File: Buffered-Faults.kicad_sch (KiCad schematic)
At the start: 4 parts, among them U6 TSB712AIDT, U7 TSB712AIDT

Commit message: completed placement:
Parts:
- renumbered U6 to U7, U7 to U8
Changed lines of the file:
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@@
 		(on_board yes)
 		(dnp no)
-		(property "Reference" "#PWR06"
+		(property "Reference" "#PWR0101"
 			(at 240.03 133.35 0)
 			(effects
@@
 			(project "Shutdown"
 				(path "/624b8e71-6fec-49ba-b7c9-b659e140fc2f/d0efc49a-1e04-47b9-bbf8-a506e96d4b4f"
-					(reference "#PWR06")
+					(reference "#PWR0101")
 					(unit 1)
 				)
@@
 		(dnp no)
 		(fields_autoplaced yes)
-		(property "Reference" "U6"
+		(property "Reference" "U7"
 			(at 255.27 124.46 0)
 			(effects
@@
 			(project "Shutdown"
 				(path "/624b8e71-6fec-49ba-b7c9-b659e140fc2f/d0efc49a-1e04-47b9-bbf8-a506e96d4b4f"
-					(reference "U6")
+					(reference "U7")
 					(unit 3)
 				)
@@
 		(on_board yes)
 		(dnp no)
-		(property "Reference" "#PWR0105"
+		(property "Reference" "#PWR0104"
 			(at 240.03 185.42 0)
 			(effects
@@
 			(project "Shutdown"
 				(path "/624b8e71-6fec-49ba-b7c9-b659e140fc2f/d0efc49a-1e04-47b9-bbf8-a506e96d4b4f"
-					(reference "#PWR0105")
+					(reference "#PWR0104")
 					(unit 1)
 				)
@@
 		(dnp no)
 		(fields_autoplaced yes)
-		(property "Reference" "U6"
+		(property "Reference" "U7"
 			(at 180.975 93.98 0)
 			(effects
@@
 			(project "Shutdown"
 				(path "/624b8e71-6fec-49ba-b7c9-b659e140fc2f/d0efc49a-1e04-47b9-bbf8-a506e96d4b4f"
-					(reference "U6")
+					(reference "U7")
 					(unit 1)
 				)
@@
 		(dnp no)
 		(fields_autoplaced yes)
-		(property "Reference" "U7"
+		(property "Reference" "U8"
 			(at 180.975 154.94 0)
 			(effects
@@
 			(project "Shutdown"
 				(path "/624b8e71-6fec-49ba-b7c9-b659e140fc2f/d0efc49a-1e04-47b9-bbf8-a506e96d4b4f"
-					(reference "U7")
+					(reference "U8")
 					(unit 1)
 				)
@@
 		(on_board yes)
 		(dnp no)
-		(property "Reference" "#PWR010"
+		(property "Reference" "#PWR0102"
 			(at 240.03 151.13 0)
 			(effects
@@
 			(project "Shutdown"
 				(path "/624b8e71-6fec-49ba-b7c9-b659e140fc2f/d0efc49a-1e04-47b9-bbf8-a506e96d4b4f"
-					(reference "#PWR010")
+					(reference "#PWR0102")
 					(unit 1)
 				)
@@
 		(dnp no)
 		(fields_autoplaced yes)
-		(property "Reference" "U7"
+		(property "Reference" "U8"
 			(at 180.975 185.42 0)
 			(effects
@@
 			(project "Shutdown"
 				(path "/624b8e71-6fec-49ba-b7c9-b659e140fc2f/d0efc49a-1e04-47b9-bbf8-a506e96d4b4f"
-					(reference "U7")
+					(reference "U8")
 					(unit 2)
 				)
@@
 		(on_board yes)
 		(dnp no)
-		(property "Reference" "#PWR011"
+		(property "Reference" "#PWR0103"
 			(at 240.03 167.64 0)
 			(effects
@@
 			(project "Shutdown"
 				(path "/624b8e71-6fec-49ba-b7c9-b659e140fc2f/d0efc49a-1e04-47b9-bbf8-a506e96d4b4f"
-					(reference "#PWR011")
+					(reference "#PWR0103")
 					(unit 1)
 				)
@@
 		(dnp no)
 		(fields_autoplaced yes)
-		(property "Reference" "U7"
+		(property "Reference" "U8"
 			(at 255.27 158.75 0)
 			(effects
@@
 			(project "Shutdown"
 				(path "/624b8e71-6fec-49ba-b7c9-b659e140fc2f/d0efc49a-1e04-47b9-bbf8-a506e96d4b4f"
-					(reference "U7")
+					(reference "U8")
 					(unit 3)
 				)
@@
 		(on_board yes)
 		(dnp no)
-		(property "Reference" "#PWR02"
+		(property "Reference" "#PWR0105"
 			(at 167.64 200.66 0)
 			(effects
@@
 			(project "Shutdown"
 				(path "/624b8e71-6fec-49ba-b7c9-b659e140fc2f/d0efc49a-1e04-47b9-bbf8-a506e96d4b4f"
-					(reference "#PWR02")
+					(reference "#PWR0105")
 					(unit 1)
 				)
@@
 		(dnp no)
 		(fields_autoplaced yes)
-		(property "Reference" "U6"
+		(property "Reference" "U7"
 			(at 180.975 124.46 0)
 			(effects
@@
 			(project "Shutdown"
 				(path "/624b8e71-6fec-49ba-b7c9-b659e140fc2f/d0efc49a-1e04-47b9-bbf8-a506e96d4b4f"
-					(reference "U6")
+					(reference "U7")
 					(unit 2)
 				)

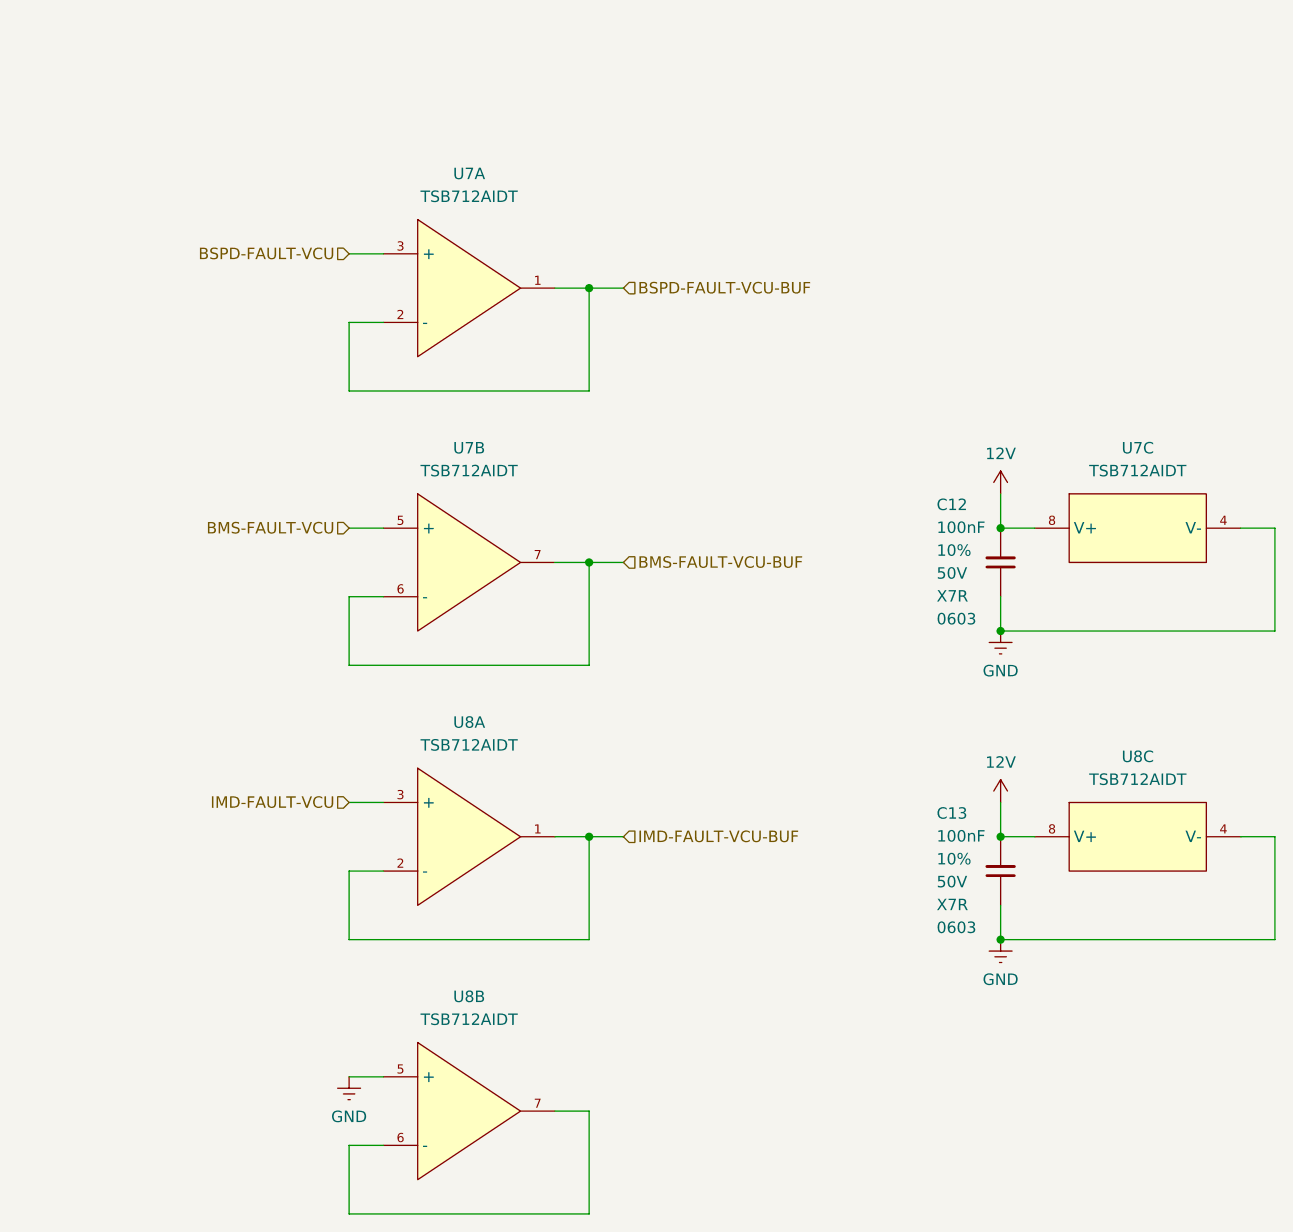
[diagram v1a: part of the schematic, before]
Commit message: changed BSPD, BMS fault logic to match Mk11 specs, all signals going back to VCU have 12V fault, 0V no fault readings, connector symbols/footprints left for next push
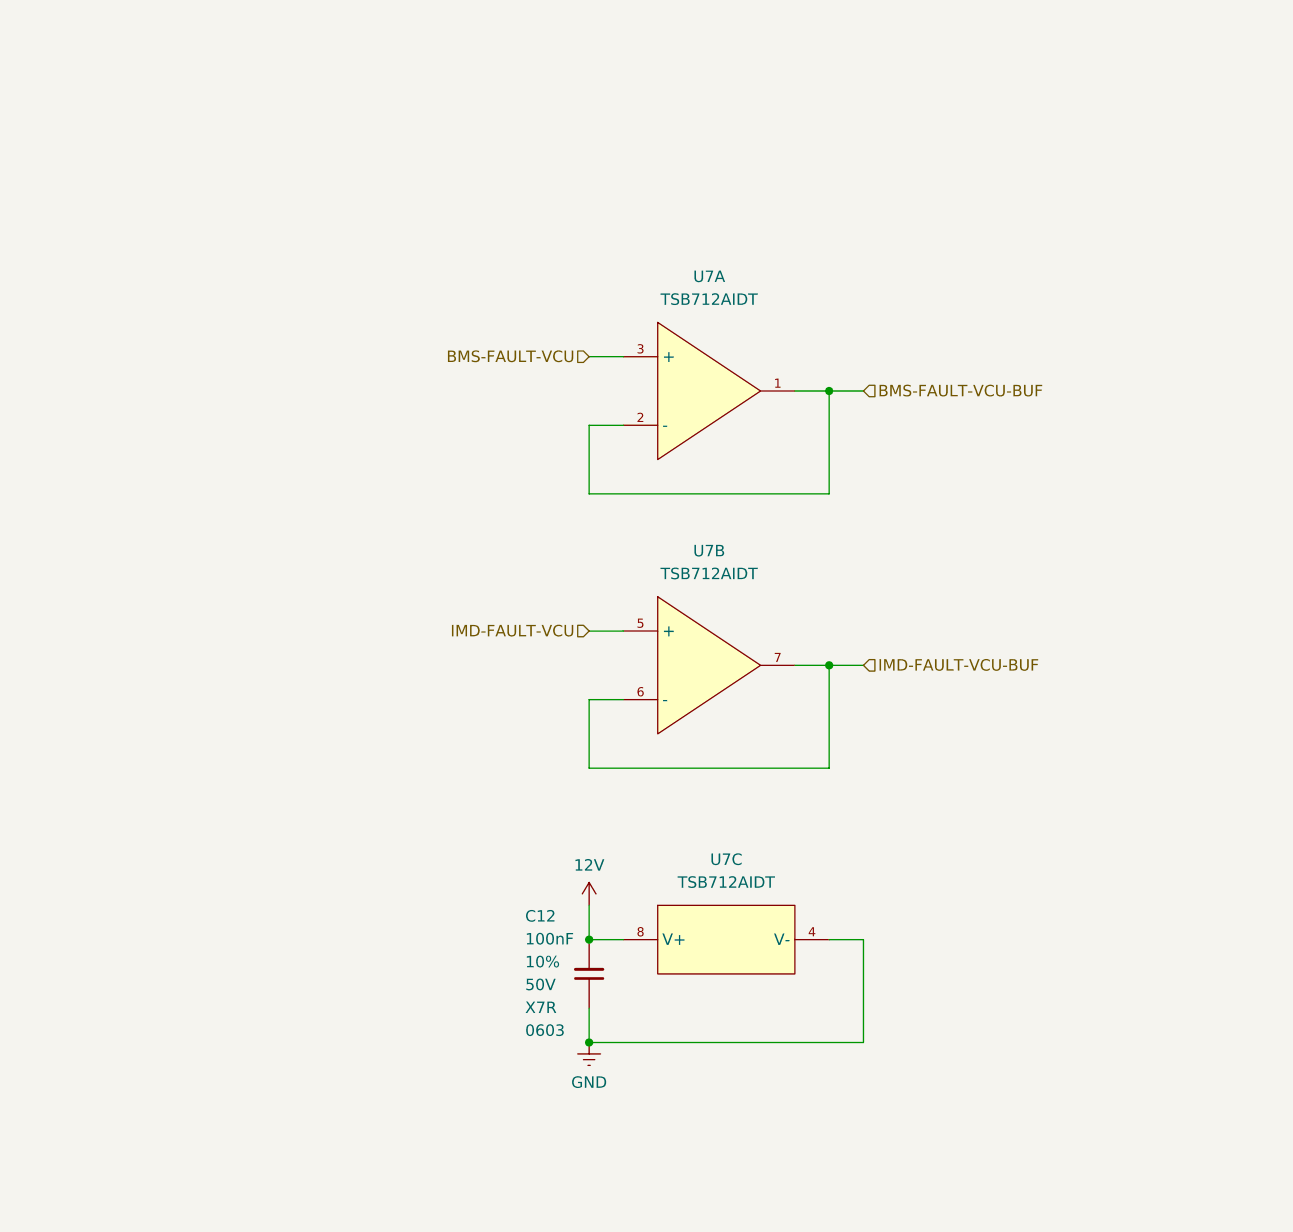
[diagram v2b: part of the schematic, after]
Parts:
- removed C13: 100nF, Capacitor_SMD:C_0603_1608Metric_Pad1.08x0.95mm_HandSolder, symbol -C-Ceramic-0603:C-0603-100nF-10%-50V-X7R
- removed U8: TSB712AIDT, Package_SO:SOIC-8_5.3x5.3mm_P1.27mm, symbol -Operational-Amplifiers:TSB712AIDT
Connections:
- net BSPD-FAULT-VCU is gone; now on net BMS-FAULT-VCU: U7.3 (+)
- net BSPD-FAULT-VCU-BUF is gone; now on net BMS-FAULT-VCU-BUF: U7.1, U7.2 (-)
- net BMS-FAULT-VCU: no longer U7.5 (+)
- net BMS-FAULT-VCU-BUF: no longer U7.6 (-), U7.7
- net IMD-FAULT-VCU: now also U7.5 (+)
- net IMD-FAULT-VCU-BUF: now also U7.6 (-), U7.7
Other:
- moved on the sheet: C12, U7A, U7B, U7C

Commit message: cleaning port names
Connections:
- net BMS-FAULT-VCU renamed BMS-FAULT
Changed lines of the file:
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@@
 		)
 	)
-	(hierarchical_label "BMS-FAULT-VCU"
+	(hierarchical_label "BMS-FAULT"
 		(shape input)
 		(at 194.31 114.3 180)

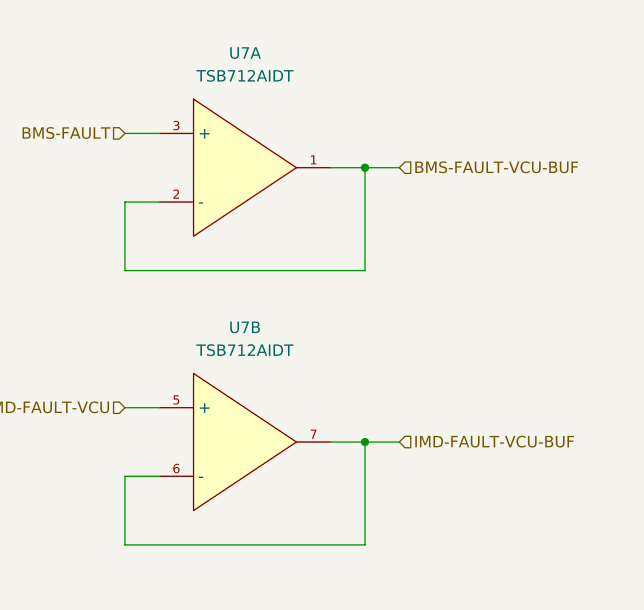
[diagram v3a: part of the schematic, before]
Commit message: updated port directionalities, updated pinout
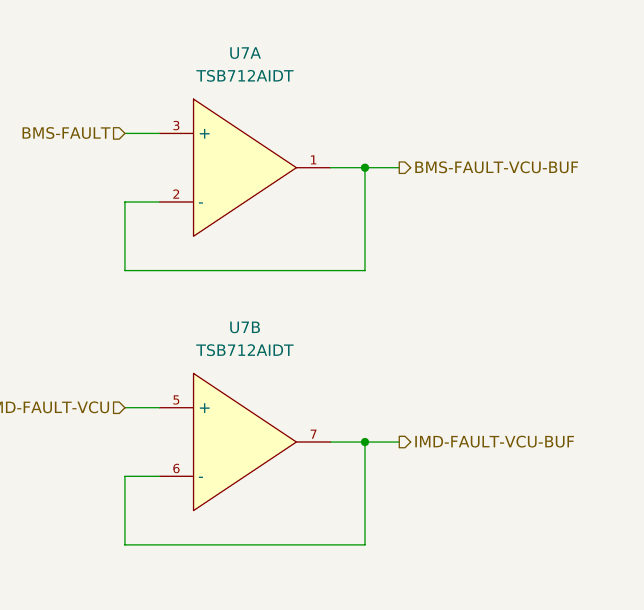
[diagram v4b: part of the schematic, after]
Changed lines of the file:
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@@
 	)
 	(hierarchical_label "IMD-FAULT-VCU-BUF"
-		(shape input)
+		(shape output)
 		(at 224.79 148.59 0)
 		(effects
@@
 	)
 	(hierarchical_label "BMS-FAULT-VCU-BUF"
-		(shape input)
+		(shape output)
 		(at 224.79 118.11 0)
 		(effects

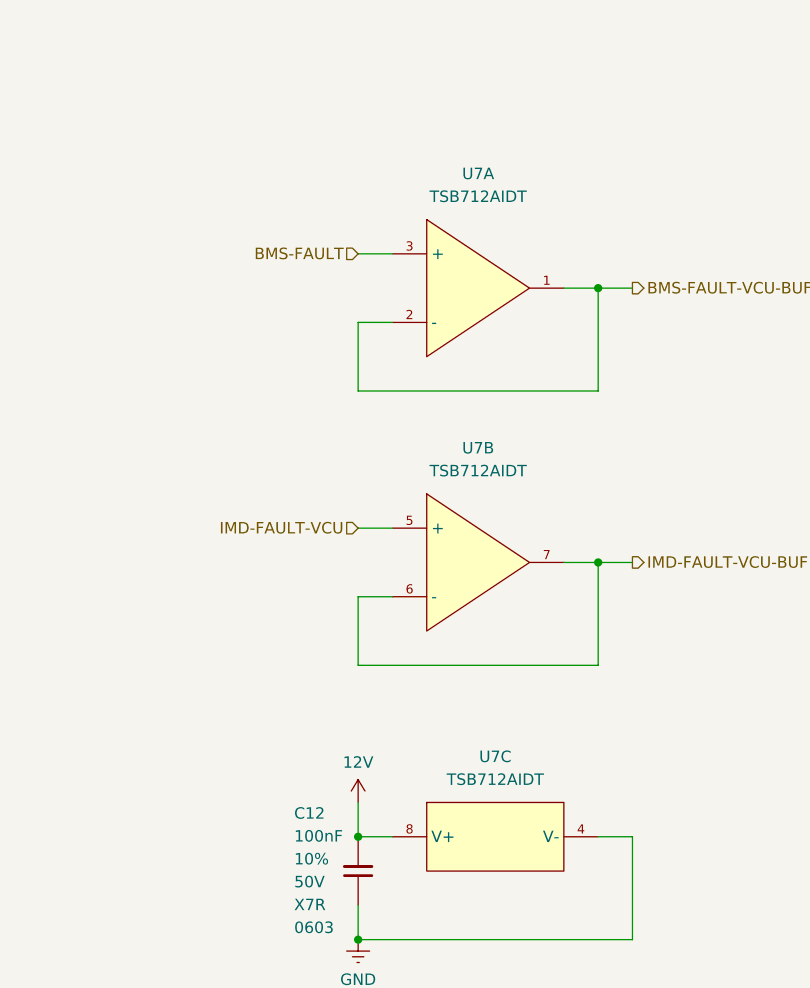
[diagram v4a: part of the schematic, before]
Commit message: Schem is reannotated time to redo all of the layout
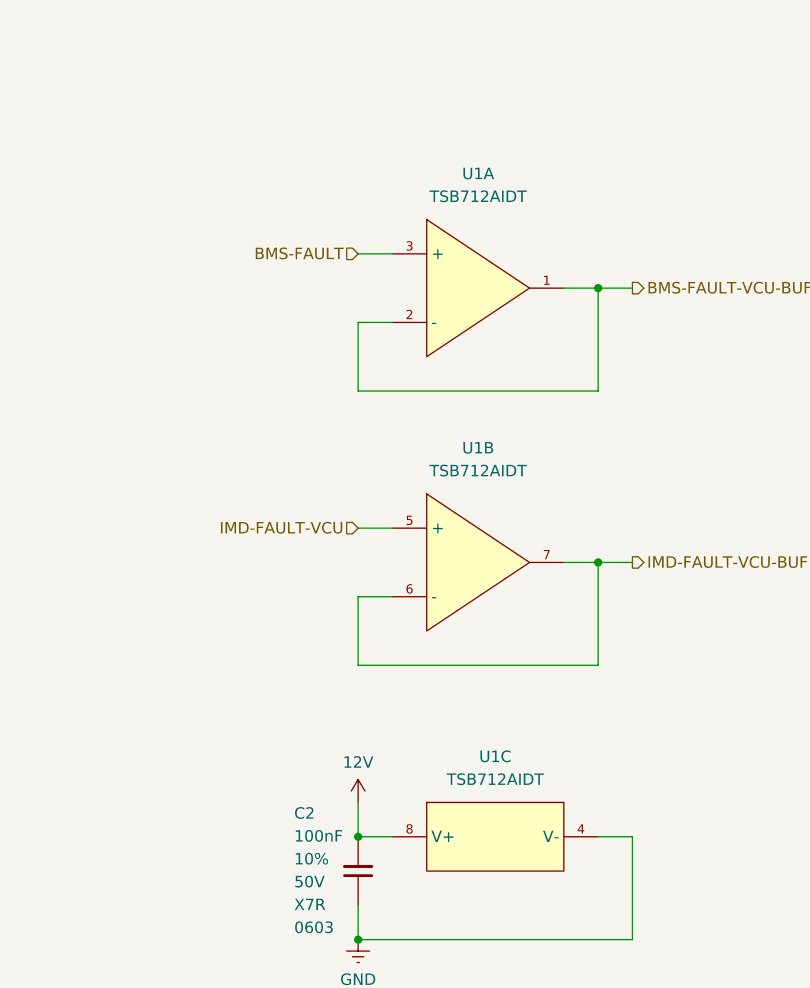
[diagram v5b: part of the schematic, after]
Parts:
- renumbered C12 to C2, U7 to U1
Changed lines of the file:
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@@
 		(on_board yes)
 		(dnp no)
-		(property "Reference" "#PWR0101"
+		(property "Reference" "#PWR063"
 			(at 194.31 179.07 0)
 			(effects
@@
 			(project "Shutdown"
 				(path "/624b8e71-6fec-49ba-b7c9-b659e140fc2f/d0efc49a-1e04-47b9-bbf8-a506e96d4b4f"
-					(reference "#PWR0101")
+					(reference "#PWR063")
 					(unit 1)
 				)
@@
 		(dnp no)
 		(fields_autoplaced yes)
-		(property "Reference" "U7"
+		(property "Reference" "U1"
 			(at 209.55 170.18 0)
 			(effects
@@
 			(project "Shutdown"
 				(path "/624b8e71-6fec-49ba-b7c9-b659e140fc2f/d0efc49a-1e04-47b9-bbf8-a506e96d4b4f"
-					(reference "U7")
+					(reference "U1")
 					(unit 3)
 				)
@@
 		(on_board yes)
 		(dnp no)
-		(property "Reference" "C12"
+		(property "Reference" "C2"
 			(at 187.1973 176.4747 90)
 			(effects
@@
 			(project "Shutdown"
 				(path "/624b8e71-6fec-49ba-b7c9-b659e140fc2f/d0efc49a-1e04-47b9-bbf8-a506e96d4b4f"
-					(reference "C12")
+					(reference "C2")
 					(unit 1)
 				)
@@
 		(dnp no)
 		(fields_autoplaced yes)
-		(property "Reference" "U7"
+		(property "Reference" "U1"
 			(at 207.645 105.41 0)
 			(effects
@@
 			(project "Shutdown"
 				(path "/624b8e71-6fec-49ba-b7c9-b659e140fc2f/d0efc49a-1e04-47b9-bbf8-a506e96d4b4f"
-					(reference "U7")
+					(reference "U1")
 					(unit 1)
 				)
@@
 		(on_board yes)
 		(dnp no)
-		(property "Reference" "#PWR0102"
+		(property "Reference" "#PWR064"
 			(at 194.31 196.85 0)
 			(effects
@@
 			(project "Shutdown"
 				(path "/624b8e71-6fec-49ba-b7c9-b659e140fc2f/d0efc49a-1e04-47b9-bbf8-a506e96d4b4f"
-					(reference "#PWR0102")
+					(reference "#PWR064")
 					(unit 1)
 				)
@@
 		(dnp no)
 		(fields_autoplaced yes)
-		(property "Reference" "U7"
+		(property "Reference" "U1"
 			(at 207.645 135.89 0)
 			(effects
@@
 			(project "Shutdown"
 				(path "/624b8e71-6fec-49ba-b7c9-b659e140fc2f/d0efc49a-1e04-47b9-bbf8-a506e96d4b4f"
-					(reference "U7")
+					(reference "U1")
 					(unit 2)
 				)

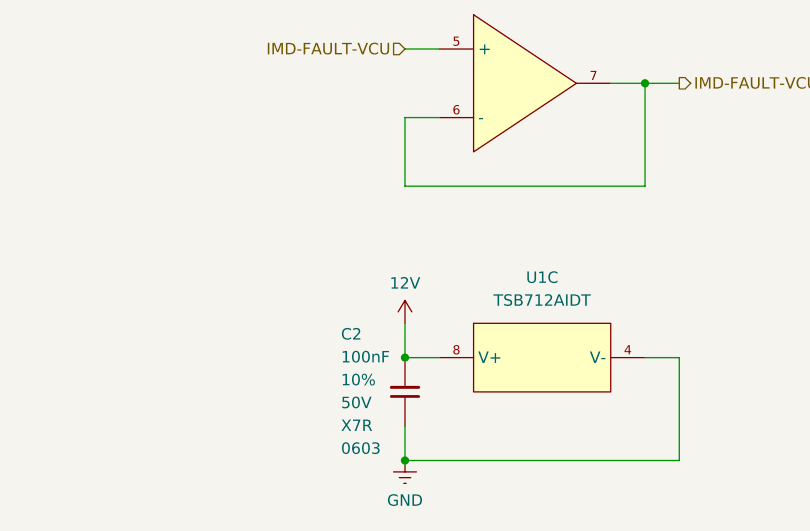
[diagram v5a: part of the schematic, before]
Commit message: Finished shutdown, 0 drc, need to export gerbers
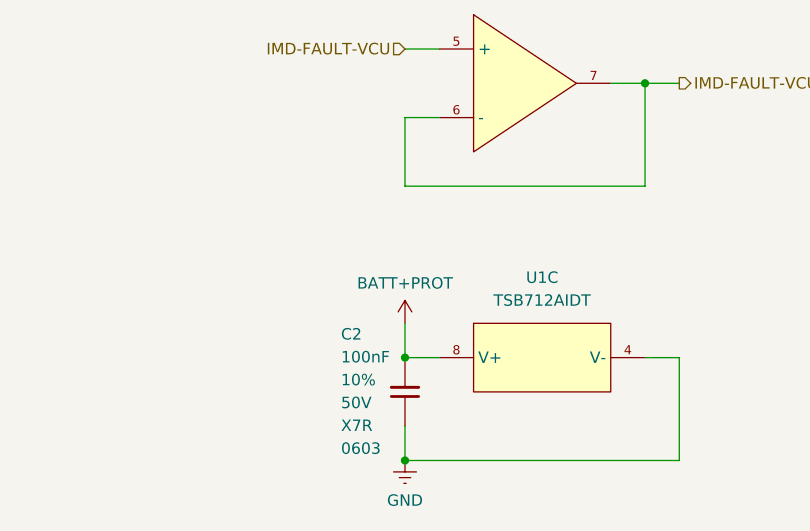
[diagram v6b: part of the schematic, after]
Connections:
- net 12V renamed BATT+PROT
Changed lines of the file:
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@@
-	)
-	(symbol
-		(lib_id "power:VCC")
-		(at 194.31 175.26 0)
-		(mirror y)
-		(unit 1)
-		(exclude_from_sim no)
-		(in_bom yes)
-		(on_board yes)
-		(dnp no)
-		(property "Reference" "#PWR063"
-			(at 194.31 179.07 0)
-			(effects
-				(font
-					(size 1.27 1.27)
-				)
-				(hide yes)
-			)
-		)
-		(property "Value" "12V"
-			(at 194.31 170.815 0)
-			(effects
-				(font
-					(size 1.27 1.27)
-				)
-			)
-		)
-		(property "Footprint" ""
-			(at 194.31 175.26 0)
-			(effects
-				(font
-					(size 1.27 1.27)
-				)
-				(hide yes)
-			)
-		)
-		(property "Datasheet" ""
-			(at 194.31 175.26 0)
-			(effects
-				(font
-					(size 1.27 1.27)
-				)
-				(hide yes)
-			)
-		)
-		(property "Description" "Power symbol creates a global label with name \"VCC\""
-			(at 194.31 175.26 0)
-			(effects
-				(font
-					(size 1.27 1.27)
-				)
-				(hide yes)
-			)
-		)
-		(pin "1"
-		)
-		(instances
-			(project "Shutdown"
-				(path "/624b8e71-6fec-49ba-b7c9-b659e140fc2f/d0efc49a-1e04-47b9-bbf8-a506e96d4b4f"
-					(reference "#PWR063")
-					(unit 1)
-				)
-			)
-		)
 	)
 	(symbol
@@
 	)
 	(symbol
+		(lib_id "power:VCC")
+		(at 194.31 175.26 0)
+		(mirror y)
+		(unit 1)
+		(exclude_from_sim no)
+		(in_bom yes)
+		(on_board yes)
+		(dnp no)
+		(property "Reference" "#PWR068"
+			(at 194.31 179.07 0)
+			(effects
+				(font
+					(size 1.27 1.27)
+				)
+				(hide yes)
+			)
+		)
+		(property "Value" "BATT+PROT"
+			(at 194.31 170.815 0)
+			(effects
+				(font
+					(size 1.27 1.27)
+				)
+			)
+		)
+		(property "Footprint" ""
+			(at 194.31 175.26 0)
+			(effects
+				(font
+					(size 1.27 1.27)
+				)
+				(hide yes)
+			)
+		)
+		(property "Datasheet" ""
+			(at 194.31 175.26 0)
+			(effects
+				(font
+					(size 1.27 1.27)
+				)
+				(hide yes)
+			)
+		)
+		(property "Description" "Power symbol creates a global label with name \"VCC\""
+			(at 194.31 175.26 0)
+			(effects
+				(font
+					(size 1.27 1.27)
+				)
+				(hide yes)
+			)
+		)
+		(pin "1"
+		)
+		(instances
+			(project "Shutdown"
+				(path "/624b8e71-6fec-49ba-b7c9-b659e140fc2f/d0efc49a-1e04-47b9-bbf8-a506e96d4b4f"
+					(reference "#PWR068")
+					(unit 1)
+				)
+			)
+		)
+	)
+	(symbol
 		(lib_id "power:Earth")
 		(at 194.31 190.5 0)
@@
 		(on_board yes)
 		(dnp no)
-		(property "Reference" "#PWR064"
+		(property "Reference" "#PWR069"
 			(at 194.31 196.85 0)
 			(effects
@@
 			(project "Shutdown"
 				(path "/624b8e71-6fec-49ba-b7c9-b659e140fc2f/d0efc49a-1e04-47b9-bbf8-a506e96d4b4f"
-					(reference "#PWR064")
+					(reference "#PWR069")
 					(unit 1)
 				)
